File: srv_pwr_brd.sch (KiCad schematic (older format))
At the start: 6 parts, among them J01 SRV1_in, J02 SRV2_in, J03 SRV3_in, J11 SRV1_out, J12 SRV2_out, J13 SRV3_out

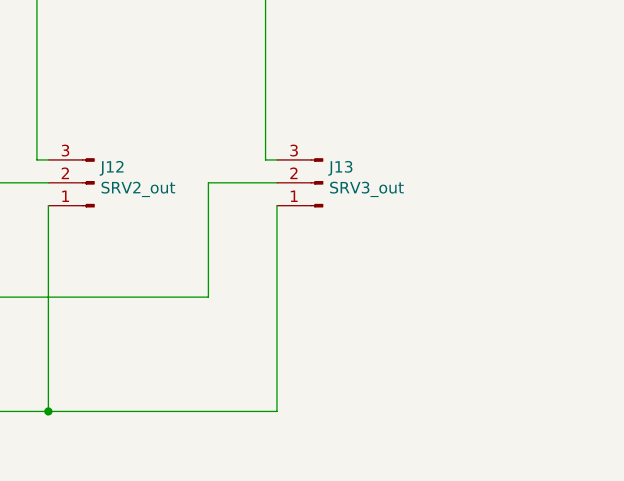
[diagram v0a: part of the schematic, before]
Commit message: add BATT header
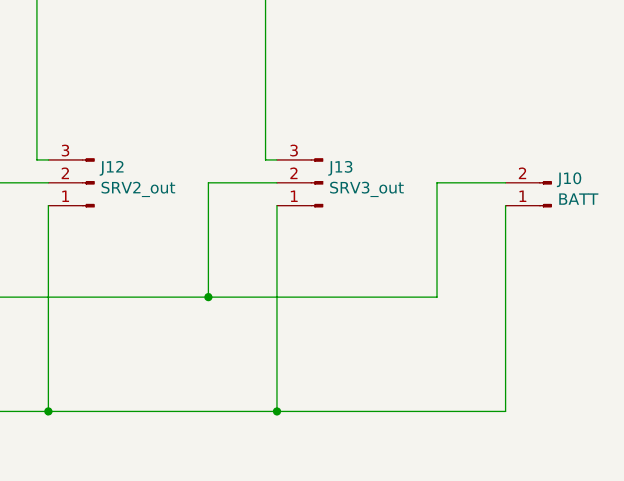
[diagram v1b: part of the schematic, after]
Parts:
- added J10: BATT, Connector_PinHeader_2.54mm:PinHeader_1x02_P2.54mm_Vertical, symbol Connector:Conn_01x02_Male
- J01, J02, J03, J11, J12, J13: footprint (none) -> Connector_PinHeader_2.54mm:PinHeader_1x03_P2.54mm_Vertical
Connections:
- net +BATT: now also J10.2 (Pin_2)
- net GND: now also J10.1 (Pin_1)
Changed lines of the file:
@@
 F 0 "J01" H 2108 2781 50  0000 R CNN
 F 1 "SRV1_in" H 2108 2690 50  0000 R CNN
-F 2 "" H 2000 2500 50  0001 C CNN
+F 2 "Connector_PinHeader_2.54mm:PinHeader_1x03_P2.54mm_Vertical" H 2000 2500 50  0001 C CNN
 F 3 "~" H 2000 2500 50  0001 C CNN
 	1    2000 2500
@@
 F 0 "J02" H 3108 2781 50  0000 R CNN
 F 1 "SRV2_in" H 3108 2690 50  0000 R CNN
-F 2 "" H 3000 2500 50  0001 C CNN
+F 2 "Connector_PinHeader_2.54mm:PinHeader_1x03_P2.54mm_Vertical" H 3000 2500 50  0001 C CNN
 F 3 "~" H 3000 2500 50  0001 C CNN
 	1    3000 2500
@@
 F 0 "J03" H 4108 2781 50  0000 R CNN
 F 1 "SRV3_in" H 4108 2690 50  0000 R CNN
-F 2 "" H 4000 2500 50  0001 C CNN
+F 2 "Connector_PinHeader_2.54mm:PinHeader_1x03_P2.54mm_Vertical" H 4000 2500 50  0001 C CNN
 F 3 "~" H 4000 2500 50  0001 C CNN
 	1    4000 2500
@@
 F 0 "J11" H 2472 3932 50  0000 R CNN
 F 1 "SRV1_out" H 2472 4023 50  0000 R CNN
-F 2 "" H 2500 4000 50  0001 C CNN
+F 2 "Connector_PinHeader_2.54mm:PinHeader_1x03_P2.54mm_Vertical" H 2500 4000 50  0001 C CNN
 F 3 "~" H 2500 4000 50  0001 C CNN
 	1    2500 4000
@@
 F 0 "J12" H 3472 3932 50  0000 R CNN
 F 1 "SRV2_out" H 3472 4023 50  0000 R CNN
-F 2 "" H 3500 4000 50  0001 C CNN
+F 2 "Connector_PinHeader_2.54mm:PinHeader_1x03_P2.54mm_Vertical" H 3500 4000 50  0001 C CNN
 F 3 "~" H 3500 4000 50  0001 C CNN
 	1    3500 4000
@@
 F 0 "J13" H 4472 3932 50  0000 R CNN
 F 1 "SRV3_out" H 4472 4023 50  0000 R CNN
-F 2 "" H 4500 4000 50  0001 C CNN
+F 2 "Connector_PinHeader_2.54mm:PinHeader_1x03_P2.54mm_Vertical" H 4500 4000 50  0001 C CNN
 F 3 "~" H 4500 4000 50  0001 C CNN
 	1    4500 4000
@@
 Wire Wire Line
 	3000 4500 4000 4500
-Wire Wire Line
-	4000 4500 4000 4000
 Wire Wire Line
 	4000 4000 4300 4000
@@
 Wire Wire Line
 	4250 3900 4300 3900
+$Comp
+L Connector:Conn_01x02_Male J10
+U 1 1 606CCF94
+P 5500 4100
+F 0 "J10" H 5472 3982 50  0000 R CNN
+F 1 "BATT" H 5472 4073 50  0000 R CNN
+F 2 "Connector_PinHeader_2.54mm:PinHeader_1x02_P2.54mm_Vertical" H 5500 4100 50  0001 C CNN
+F 3 "~" H 5500 4100 50  0001 C CNN
+	1    5500 4100
+	-1   0    0    1
+$EndComp
+Wire Wire Line
+	4000 4500 4000 4000
+Wire Wire Line
+	4000 4500 5000 4500
+Wire Wire Line
+	5000 4500 5000 4000
+Wire Wire Line
+	5000 4000 5300 4000
+Connection ~ 4000 4500
+Wire Wire Line
+	5300 4100 5300 5000
+Wire Wire Line
+	5300 5000 4300 5000
+Connection ~ 4300 5000
 $EndSCHEMATC
